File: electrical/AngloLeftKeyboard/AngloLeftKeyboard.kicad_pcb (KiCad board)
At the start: 2 copper layers, 82 x 60 mm, 47 parts, among them J1 I2C, J2 TC2030-NL, U1 DRV5053VAQDBZR, U10 DRV5053VAQDBZR, U11 DRV5053VAQDBZR, U12 DRV5053VAQDBZR, U13 DRV5053VAQDBZR, U14 DRV5053VAQDBZR, U15 DRV5053VAQDBZR, U16 STM32L072CBTx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

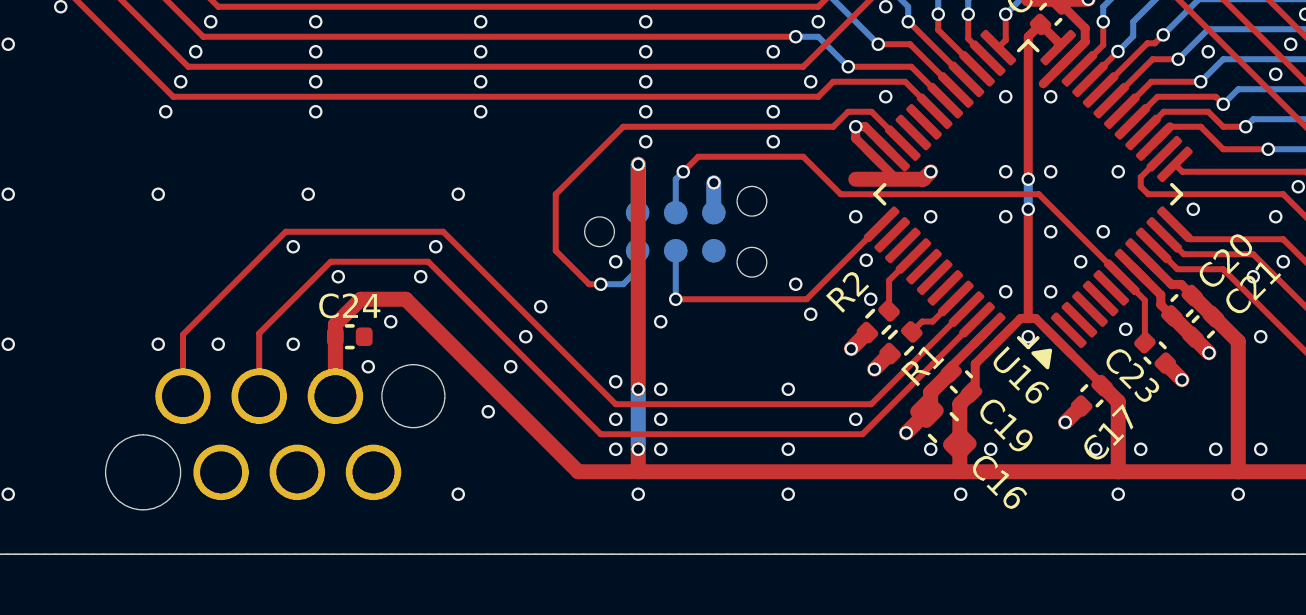
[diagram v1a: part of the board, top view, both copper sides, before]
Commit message: Change i2c cable pinout to keep signals between grounds
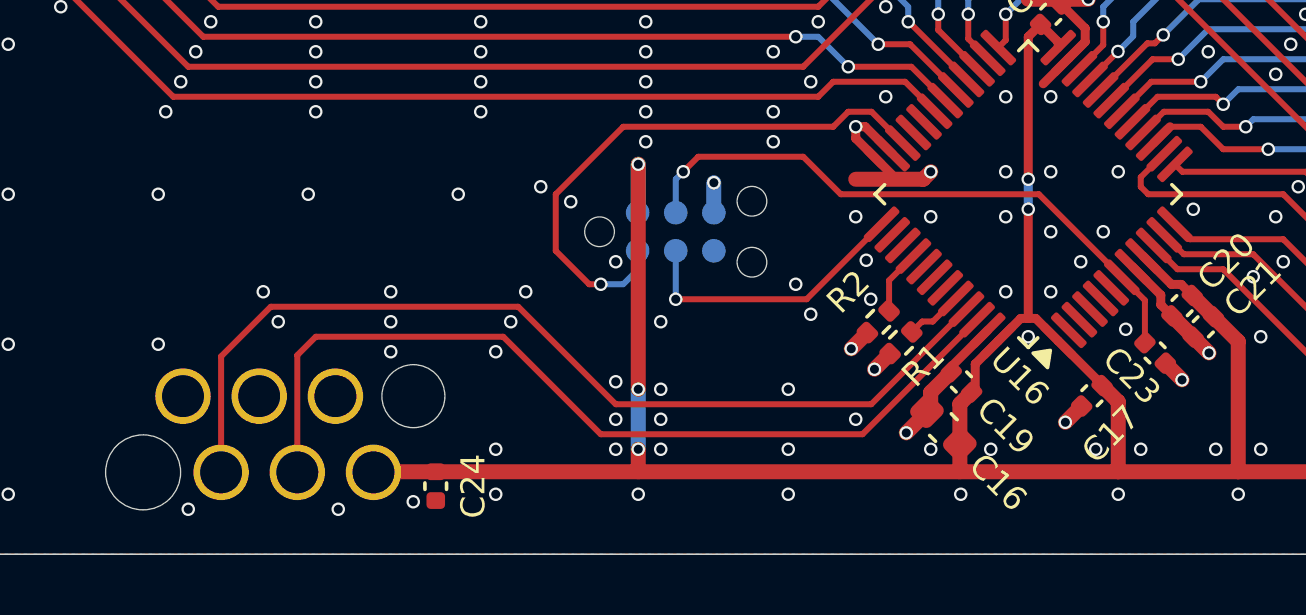
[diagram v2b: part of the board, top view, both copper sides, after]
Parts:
- moved C24 5.75 mm to (69.2, 160.7), turned to -90 degrees
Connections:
- J1 pad 1: I2C_SCL -> GND
- J1 pad 2: GND -> I2C_SCL
- J1 pad 3: I2C_SDA -> GND
- J1 pad 4: GND -> I2C_SDA
- J1 pad 5: +3.3V -> GND
- J1 pad 6: GND -> +3.3V
- J2 pad 6: (no net) -> unconnected-(J2-SWO-Pad6)
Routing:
- net +3.3V: track 113.9 -> 107.6 mm
- net I2C_SDA: track 31.0 -> 29.7 mm
- net I2C_SCL: track 33.3 -> 32.1 mm
- net GND: vias 528 -> 530
